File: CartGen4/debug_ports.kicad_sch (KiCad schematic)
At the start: 3 parts, among them J2 Conn_01x05_Male, J3 Conn_02x10_Odd_Even

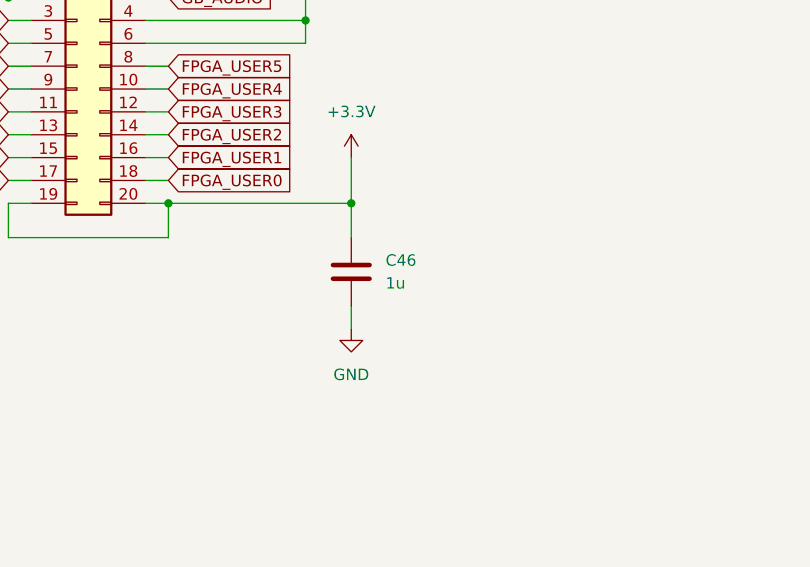
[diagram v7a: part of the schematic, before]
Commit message: Updated some component fields
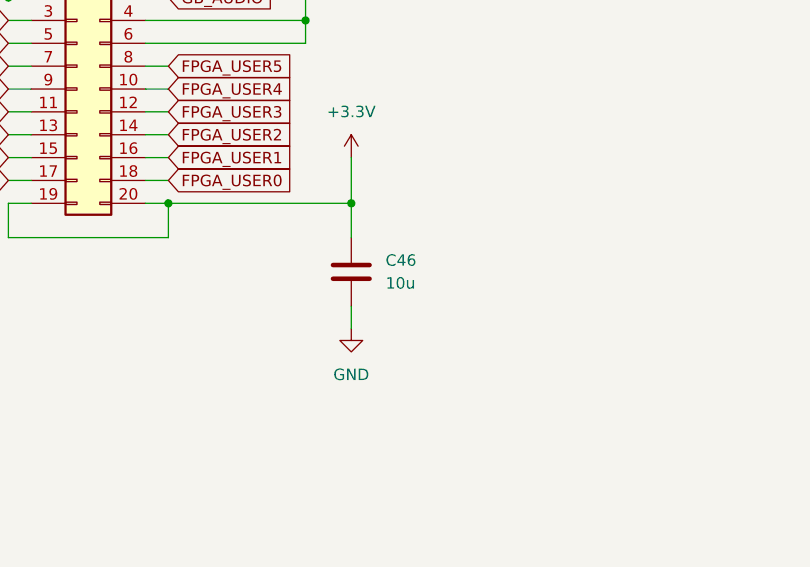
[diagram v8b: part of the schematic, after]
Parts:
- C46: value 1u -> 10u; Supplier suggestion (none) -> https://nl.mouser.com/ProductDetail/Samsung-Electro-Mechani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; Tolerance (none) -> 20%; Voltage (none) -> 10V
- J2: Supplier suggestion (none) -> https://nl.mouser.com/ProductDetail/Harwin/M50-3030542?qs=%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
- J3: Supplier suggestion (none) -> https://nl.aliexpress.com/item/4000280789459.html?spm=a2g0o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
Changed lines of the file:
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@@
+      (effects (font (size 1.27 1.27)) hide)
+    )
+    (property "Supplier suggestion" "https://nl.aliexpress.com/item/4000280789459.html?spm=a2g0o.order_list.order_list_main.10.7b0279d22xo7Wf&gatewayAdapt=glo2nld https://nl.aliexpress.com/item/1005001422512765.html?spm=a2g0o.order_list.order_list_main.11.2d4c79d2Q0rFex&gatewayAdapt=glo2nld" (id 11) (at 195.58 97.79 0)
       (effects (font (size 1.27 1.27)) hide)
     )
@@
       (effects (font (size 1.27 1.27)) (justify left))
     )
-    (property "Value" "1u" (id 1) (at 229.87 119.3799 0)
+    (property "Value" "10u" (id 1) (at 229.87 119.3799 0)
       (effects (font (size 1.27 1.27)) (justify left))
     )
@@
     )
     (property "Package ID" "0603" (id 10) (at 226.06 118.11 0)
+      (effects (font (size 1.27 1.27)) hide)
+    )
+    (property "Supplier suggestion" "https://nl.mouser.com/ProductDetail/Samsung-Electro-Mechanics/CL10A106KQ8NNNL?qs=xZ%2FP%252Ba9zWqaes9JKSsob2Q%3D%3D" (id 11) (at 226.06 118.11 0)
+      (effects (font (size 1.27 1.27)) hide)
+    )
+    (property "Tolerance" "20%" (id 12) (at 226.06 118.11 0)
+      (effects (font (size 1.27 1.27)) hide)
+    )
+    (property "Voltage" "10V" (id 13) (at 226.06 118.11 0)
       (effects (font (size 1.27 1.27)) hide)
     )
@@
       (effects (font (size 1.27 1.27)) hide)
     )
+    (property "Supplier suggestion" "https://nl.mouser.com/ProductDetail/Harwin/M50-3030542?qs=%252BdQmOuGyFcEea1rf%2Fn%2FOkw%3D%3D https://nl.mouser.com/ProductDetail/Harwin/M50-3530542?qs=%252BdQmOuGyFcHDSISYjHIhxg%3D%3D" (id 11) (at 68.58 95.25 0)
+      (effects (font (size 1.27 1.27)) hide)
+    )
